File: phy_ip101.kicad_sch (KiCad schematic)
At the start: 5 parts

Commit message: Organizado a folha da power supply
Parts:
- removed C11: (no value), symbol Device:C
- added C12: (no value), symbol Device:C
- added C13, C15, C16: (no value), Capacitor_SMD:C_0402_1005Metric_Pad0.74x0.62mm_HandSolder, symbol Device:C
- added SW1: (no value), symbol Switch:SW_Push
- added SW2: SW_Push, Button_Switch_SMD:SW_SPST_CK_RS282G05A3, symbol Switch:SW_Push
- C14: renamed from C12; footprint (none) -> Capacitor_SMD:C_0402_1005Metric_Pad0.74x0.62mm_HandSolder
- R13: value (none) -> 10k
- U3: value ~ -> (none)
- U4: value (none) -> ESP32-WROOM-32D; footprint (none) -> RF_Module:ESP32-WROOM-32
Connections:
- net +3V3: now also C12.2, C13.2
- net GNDREF: now also C12.1, C13.1, C15.2, C16.2, SW1.1, SW2.1
- net ENABLE: now reaches C14.2, R13.2, U4.3 (EN)
- net ENABLE: now also C15.1, SW1.2
- net IO0: now reaches U4.25 (IO0)
- net IO0: now also C16.1, SW2.2
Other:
- note added: "ESP32 MODULE"
- note added: "IP101 PHY ETHERNET"
- note added: "SWITCH BUTTON"
- moved on the sheet: C14, R13, U3, U4

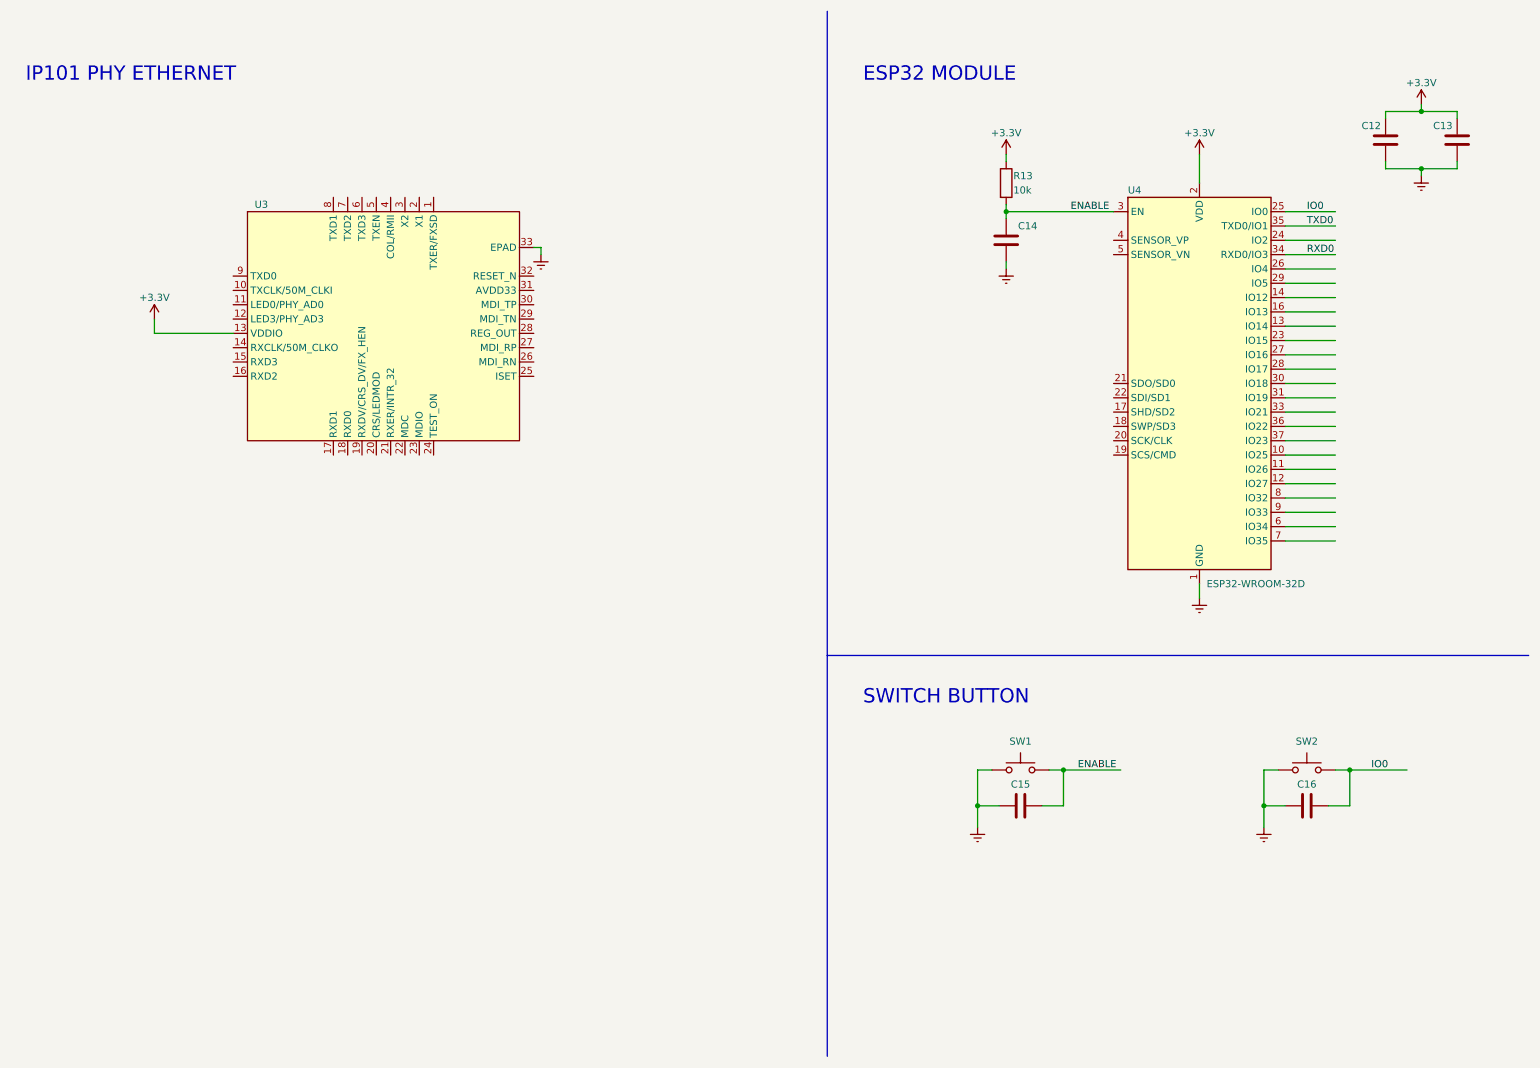
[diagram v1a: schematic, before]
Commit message: Iniciando o circuito do PHY Ethernet
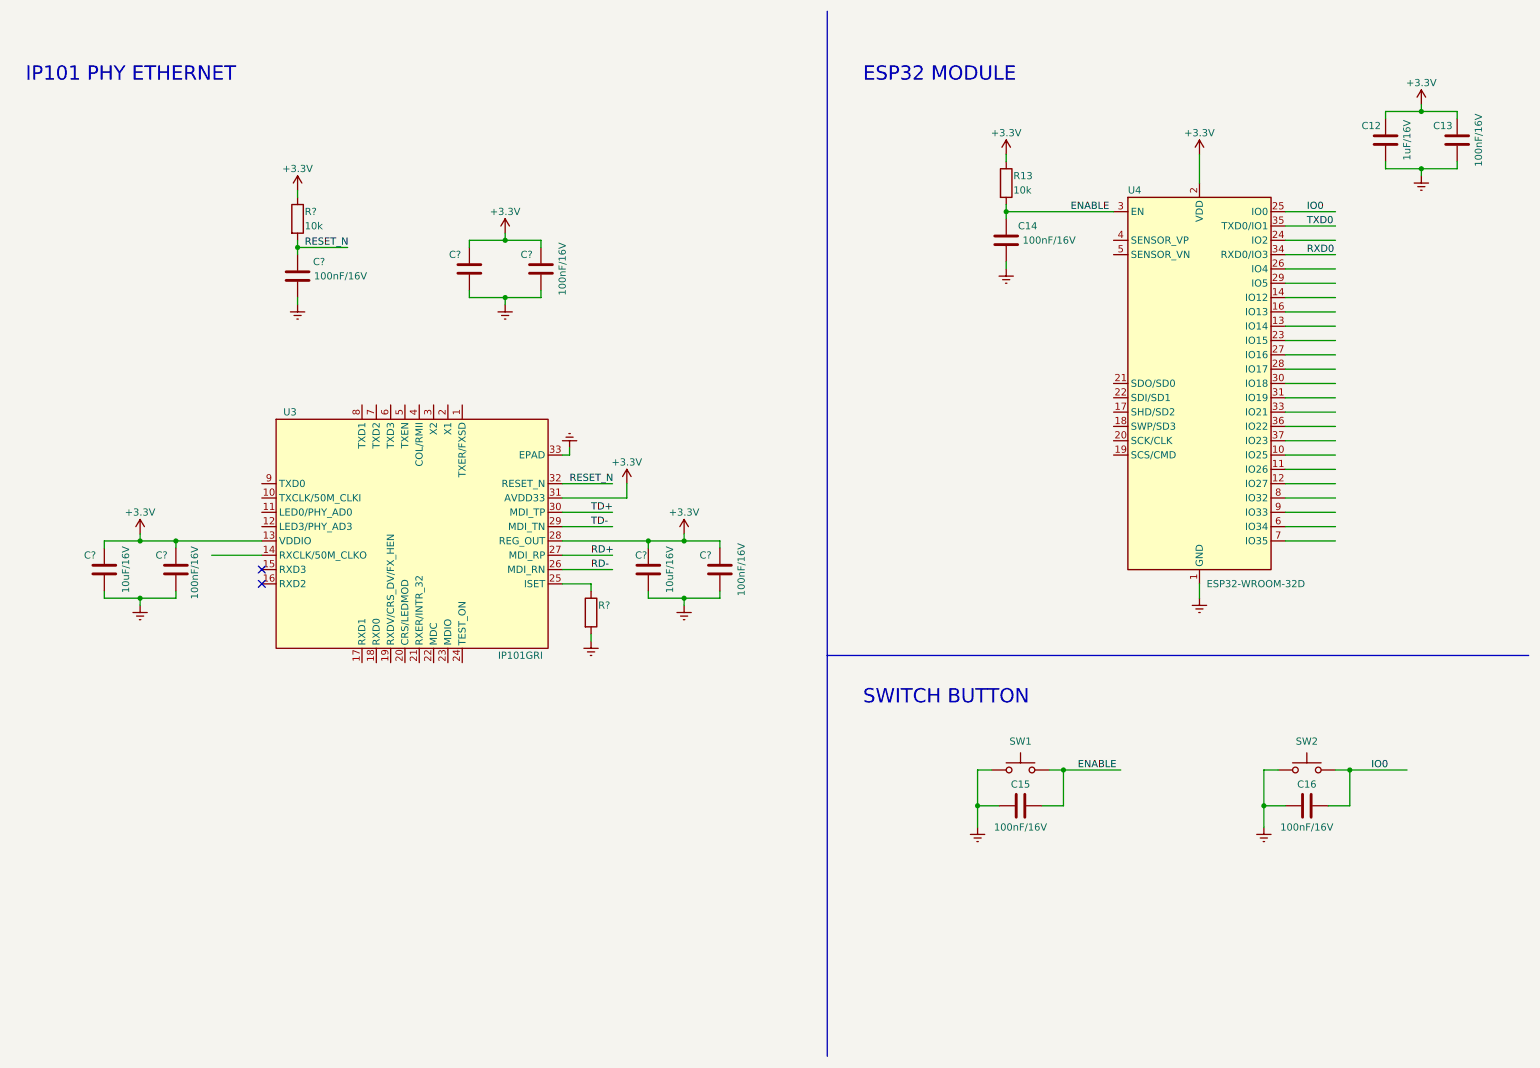
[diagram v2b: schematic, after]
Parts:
- added C? (x4): 100nF/16V, Capacitor_SMD:C_0402_1005Metric_Pad0.74x0.62mm_HandSolder, symbol Device:C
- added C? (x2): 10uF/16V, Capacitor_SMD:C_0603_1608Metric_Pad1.08x0.95mm_HandSolder, symbol Device:C
- added C?: (no value), symbol Device:C
- added R?: 10k, symbol Device:R
- added R?: (no value), symbol Device:R
- C12: value (none) -> 1uF/16V; footprint (none) -> Capacitor_SMD:C_0603_1608Metric_Pad1.08x0.95mm_HandSolder
- C13, C14, C15, C16: value (none) -> 100nF/16V
- SW1: value (none) -> SW_Push; footprint (none) -> Button_Switch_SMD:SW_SPST_CK_RS282G05A3
- U3: value (none) -> IP101GRI; footprint (none) -> Package_DFN_QFN:QFN-32-1EP_4x4mm_P0.4mm_EP2.9x2.9mm_ThermalVias
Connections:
- net +3V3: now also U3.28 (REG_OUT), U3.31 (AVDD33), C?.2, C?.2, C?.2, C?.2, C?.2, C?.2, R?.1
- net GNDREF: now also C?.1, C?.1, C?.1, C?.1, C?.1, C?.1, C?.1, R?.2
- net at U3.25 (ISET): now also R?.1
- net RD-: now reaches U3.26 (MDI_RN)
- net RD+: now reaches U3.27 (MDI_RP)
- net TD-: now reaches U3.29 (MDI_TN)
- net TD+: now reaches U3.30 (MDI_TP)
- net RESET_N: now reaches U3.32 (RESET_N)
- net RESET_N: now also C?.2, R?.2
- no-connect marks 0 -> 2
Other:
- moved on the sheet: U3

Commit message: Continuando o circuito do PHY Ethernet
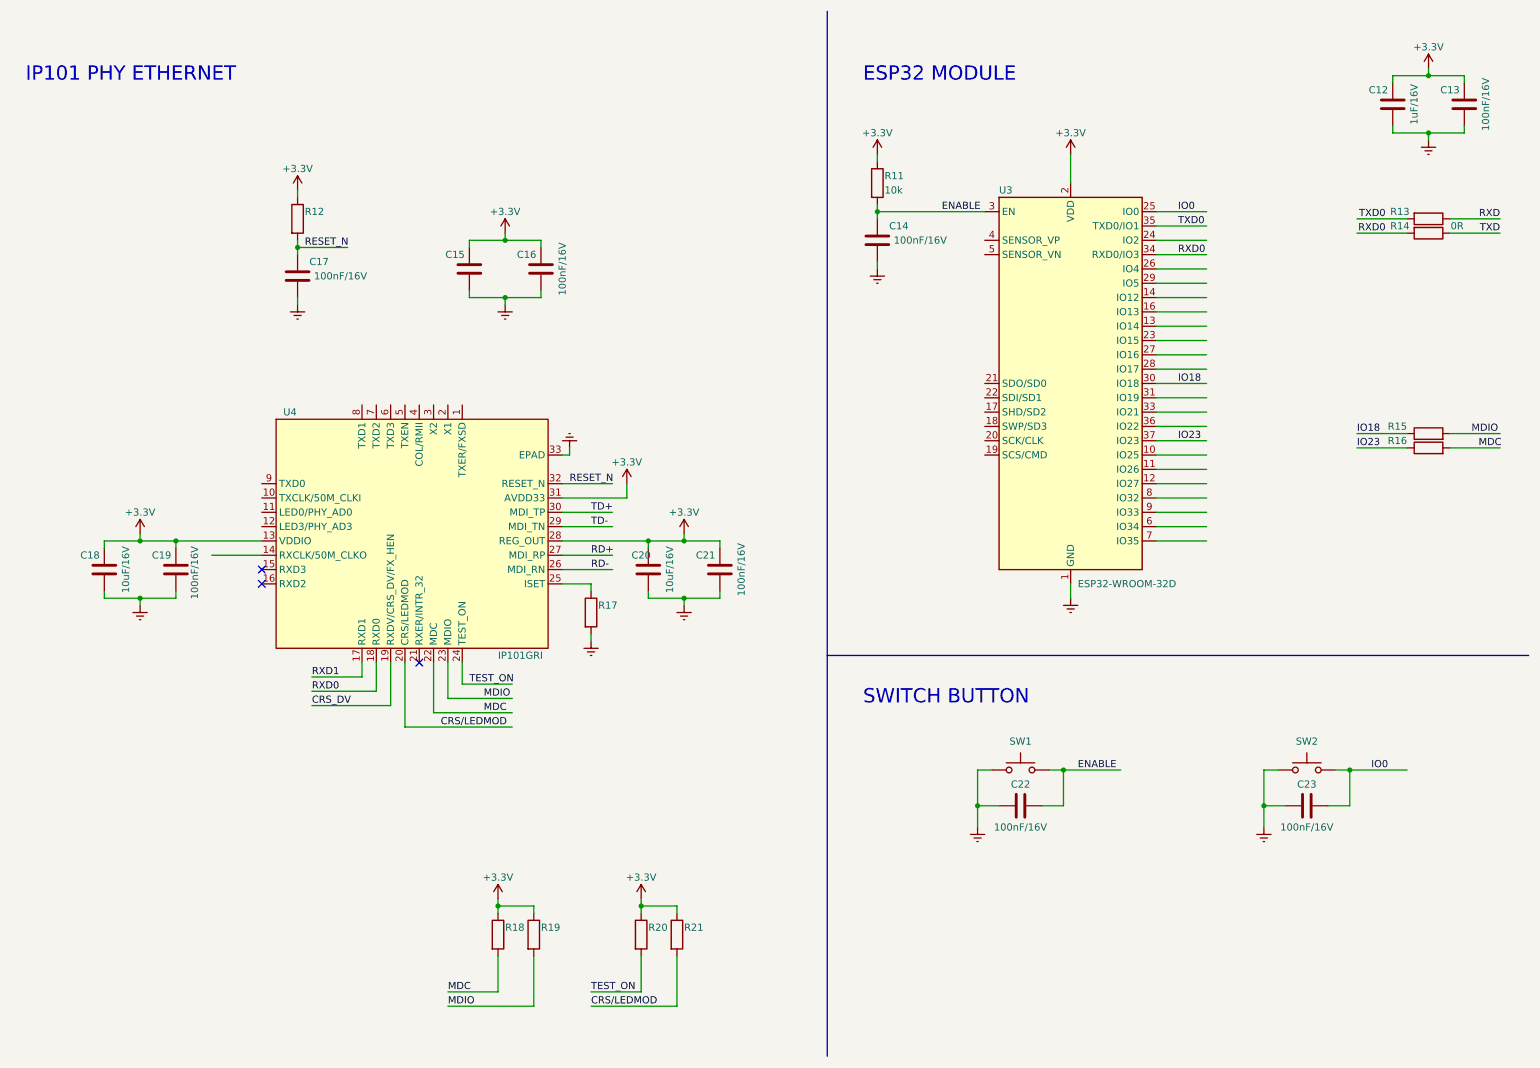
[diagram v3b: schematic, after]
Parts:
- added R13, R15, R16, R18, R19, R20, R21: (no value), symbol Device:R
- added R14: 0R, Resistor_SMD:R_0402_1005Metric_Pad0.72x0.64mm_HandSolder, symbol Device:R
- R12: renamed from R?; value 10k -> (none)
- gave numbers to parts that had none: 8
- renumbered C15 to C22, C16 to C23, R13 to R11, U4 to U3, U3 to U4
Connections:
- net +3V3: now also R18.1, R19.1, R20.1, R21.1
- net RXD0: now also U4.18 (RXD0), R14.2
- net TXD0: now also R13.2
- net RXD1: now reaches U4.17 (RXD1)
- net CRS_DV: now reaches U4.19 (RXDV/CRS_DV/FX_HEN)
- net CRS/LEDMOD: now reaches U4.20 (CRS/LEDMOD)
- net CRS/LEDMOD: now also R21.2
- net MDC: now reaches U4.22 (MDC)
- net MDC: now also R16.2, R18.2
- net MDIO: now reaches U4.23 (MDIO)
- net MDIO: now also R15.2, R19.2
- net TEST_ON: now reaches U4.24 (TEST_ON)
- net TEST_ON: now also R20.2
- net IO18: now reaches U3.30 (IO18)
- net IO18: now also R15.1
- net IO23: now reaches U3.37 (IO23)
- net IO23: now also R16.1
- new net RXD: R13.1
- new net TXD: R14.1
- no-connect marks 2 -> 3
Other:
- moved on the sheet: C12, C13, C14, R11, U3

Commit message: Continuando com o projeto do circuito do PHY Ethernet
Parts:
- added C? (x2): 15pF/50V, Capacitor_SMD:C_0402_1005Metric_Pad0.74x0.62mm_HandSolder, symbol Device:C
- added R? (x3): 5.1k, Resistor_SMD:R_0402_1005Metric_Pad0.72x0.64mm_HandSolder, symbol Device:R
- added R? (x3): 0R, Resistor_SMD:R_0402_1005Metric_Pad0.72x0.64mm_HandSolder, symbol Device:R
- added X?: ASE-xxxMHz, Oscillator:Oscillator_SMD_Abracon_ASE-4Pin_3.2x2.5mm, symbol Oscillator:ASE-xxxMHz
- C15: value (none) -> 10uF/16V; footprint (none) -> Capacitor_SMD:C_0603_1608Metric_Pad1.08x0.95mm_HandSolder
- R12: value (none) -> 10k; footprint (none) -> Resistor_SMD:R_0402_1005Metric_Pad0.72x0.64mm_HandSolder
- R13, R15, R16: value (none) -> 0R; footprint (none) -> Resistor_SMD:R_0402_1005Metric_Pad0.72x0.64mm_HandSolder
- R17: value (none) -> 6.19k; footprint (none) -> Resistor_SMD:R_0402_1005Metric_Pad0.72x0.64mm_HandSolder
- R18, R19, R20, R21: value (none) -> 5.1k; footprint (none) -> Resistor_SMD:R_0402_1005Metric_Pad0.72x0.64mm_HandSolder
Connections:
- net +3V3: now also R?.1
- net GNDREF: now also C?.1, C?.1, R?.1, R?.1, X?.2 (GND), X?.4 (Vdd)
- net TEST_ON: now also R?.2
- net TXD0: now also U4.9 (TXD0), R?.2
- net TXER/FXSD: now reaches U4.1 (TXER/FXSD)
- net TXER/FXSD: now also R?.2
- net X1: now reaches U4.2 (X1)
- net X1: now also C?.2, X?.1 (EN)
- net X2: now reaches U4.3 (X2)
- net X2: now also C?.2, X?.3 (OUT)
- net COL/RMII: now reaches U4.4 (COL/RMII)
- net COL/RMII: now also R?.2
- net TXEN: now reaches U4.5 (TXEN)
- net TXEN: now also R?.2
- net TXD1: now reaches U4.8 (TXD1)
- net TXD1: now also R?.2
- net IO19: now reaches U3.31 (IO19)
- net IO19: now also R?.1
- net IO21: now reaches U3.33 (IO21)
- net IO21: now also R?.1
- net IO22: now reaches U3.36 (IO22)
- net IO22: now also R?.1
- no-connect marks 3 -> 5
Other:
- moved on the sheet: C15, C16, C17, R12, R16, R18, R19, R20, R21
